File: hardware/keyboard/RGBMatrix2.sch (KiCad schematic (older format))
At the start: 29 parts

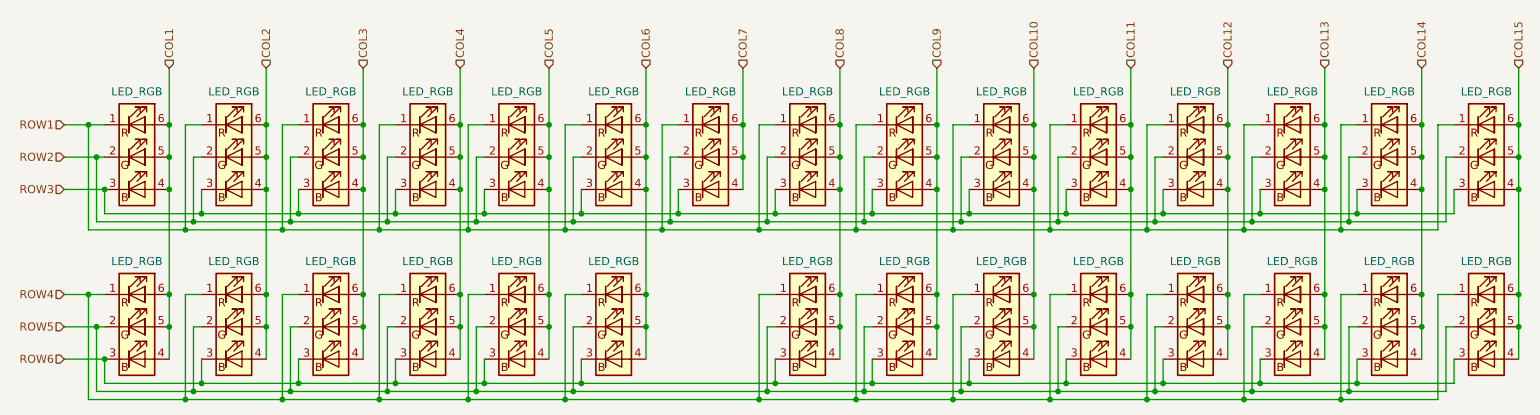
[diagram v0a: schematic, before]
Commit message: switch to proper type of RGB(Common anode)
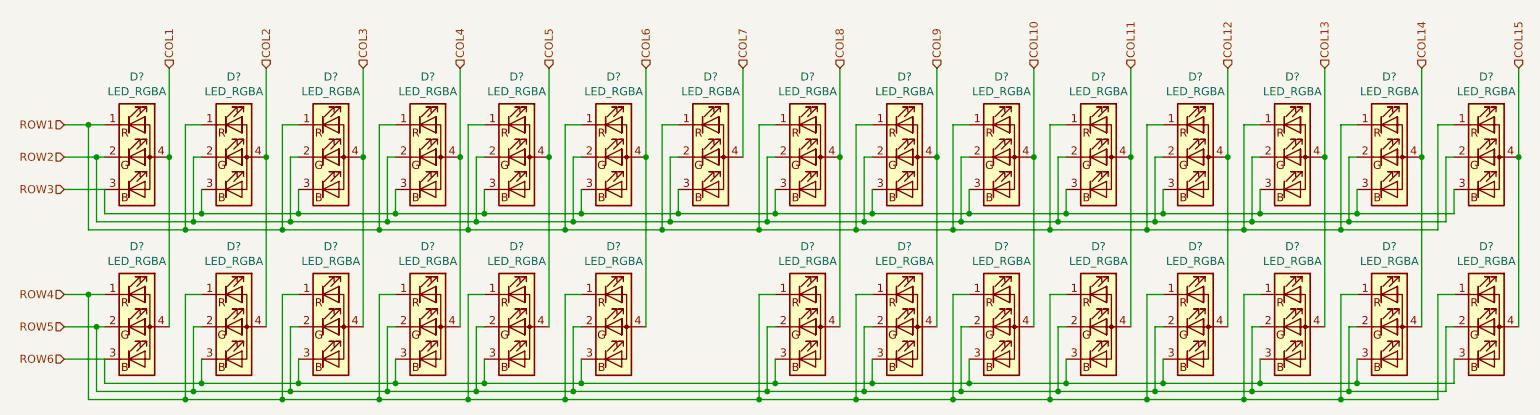
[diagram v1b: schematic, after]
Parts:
- removed D114, D115, D116, D117, D118, D119, D120, D121, D122, D123, D124, D125, D126, D128, D129, D130, D131, D132, D133, D134, D135, D136, D137, D138, D139, D140, D141, D142, D143: LED_RGB, symbol Device:LED_RGB
- added D? (x29): LED_RGBA, symbol Device:LED_RGBA
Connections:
- net COL1: now also D?.4 (A), D?.4 (A)
- net COL10: now also D?.4 (A), D?.4 (A)
- net COL11: now also D?.4 (A), D?.4 (A)
- net COL12: now also D?.4 (A), D?.4 (A)
- net COL13: now also D?.4 (A), D?.4 (A)
- net COL14: now also D?.4 (A), D?.4 (A)
- net COL15: now also D?.4 (A), D?.4 (A)
- net COL2: now also D?.4 (A), D?.4 (A)
- net COL3: now also D?.4 (A), D?.4 (A)
- net COL4: now also D?.4 (A), D?.4 (A)
- net COL5: now also D?.4 (A), D?.4 (A)
- net COL6: now also D?.4 (A), D?.4 (A)
- net COL7: now also D?.4 (A)
- net COL8: now also D?.4 (A), D?.4 (A)
- net COL9: now also D?.4 (A), D?.4 (A)
- net ROW1: now also D?.1 (RK), D?.1 (RK), D?.1 (RK), D?.1 (RK), D?.1 (RK), D?.1 (RK), D?.1 (RK), D?.1 (RK), D?.1 (RK), D?.1 (RK), D?.1 (RK), D?.1 (RK), D?.1 (RK), D?.1 (RK), D?.1 (RK)
- net ROW2: now also D?.2 (GK), D?.2 (GK), D?.2 (GK), D?.2 (GK), D?.2 (GK), D?.2 (GK), D?.2 (GK), D?.2 (GK), D?.2 (GK), D?.2 (GK), D?.2 (GK), D?.2 (GK), D?.2 (GK), D?.2 (GK), D?.2 (GK)
- net ROW3: now also D?.3 (BK), D?.3 (BK), D?.3 (BK), D?.3 (BK), D?.3 (BK), D?.3 (BK), D?.3 (BK), D?.3 (BK), D?.3 (BK), D?.3 (BK), D?.3 (BK), D?.3 (BK), D?.3 (BK), D?.3 (BK), D?.3 (BK)
- net ROW4: now also D?.1 (RK), D?.1 (RK), D?.1 (RK), D?.1 (RK), D?.1 (RK), D?.1 (RK), D?.1 (RK), D?.1 (RK), D?.1 (RK), D?.1 (RK), D?.1 (RK), D?.1 (RK), D?.1 (RK), D?.1 (RK)
- net ROW5: now also D?.2 (GK), D?.2 (GK), D?.2 (GK), D?.2 (GK), D?.2 (GK), D?.2 (GK), D?.2 (GK), D?.2 (GK), D?.2 (GK), D?.2 (GK), D?.2 (GK), D?.2 (GK), D?.2 (GK), D?.2 (GK)
- net ROW6: now also D?.3 (BK), D?.3 (BK), D?.3 (BK), D?.3 (BK), D?.3 (BK), D?.3 (BK), D?.3 (BK), D?.3 (BK), D?.3 (BK), D?.3 (BK), D?.3 (BK), D?.3 (BK), D?.3 (BK), D?.3 (BK)

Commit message: fix unconnected rgb
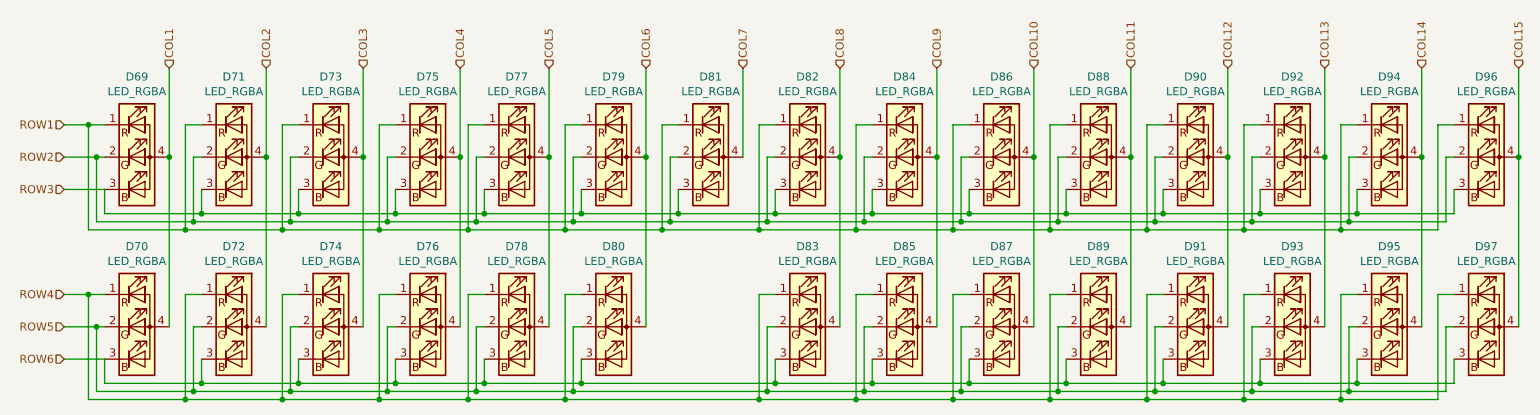
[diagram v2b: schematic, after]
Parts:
- gave numbers to parts that had none: 29
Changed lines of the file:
@@
 U 1 1 5ECE6F4E
 P 1750 2400
-F 0 "D?" H 1750 2897 50  0000 C CNN
+AR Path="/5EC33E3D/5EC48B37/5ECE6F4E" Ref="D?"  Part="1"
+AR Path="/5EC33E3D/5E12F961/5ECE6F4E" Ref="D69"  Part="1"
+F 0 "D69" H 1750 2897 50  0000 C CNN
 F 1 "LED_RGBA" H 1750 2806 50  0000 C CNN
 F 2 "" H 1750 2350 50  0001 C CNN
@@
 U 1 1 5ECF7D8D
 P 2350 2400
-F 0 "D?" H 2350 2897 50  0000 C CNN
+AR Path="/5EC33E3D/5EC48B37/5ECF7D8D" Ref="D?"  Part="1"
+AR Path="/5EC33E3D/5E12F961/5ECF7D8D" Ref="D71"  Part="1"
+F 0 "D71" H 2350 2897 50  0000 C CNN
 F 1 "LED_RGBA" H 2350 2806 50  0000 C CNN
 F 2 "" H 2350 2350 50  0001 C CNN
@@
 U 1 1 5ED08C1C
 P 2950 2400
-F 0 "D?" H 2950 2897 50  0000 C CNN
+AR Path="/5EC33E3D/5EC48B37/5ED08C1C" Ref="D?"  Part="1"
+AR Path="/5EC33E3D/5E12F961/5ED08C1C" Ref="D73"  Part="1"
+F 0 "D73" H 2950 2897 50  0000 C CNN
 F 1 "LED_RGBA" H 2950 2806 50  0000 C CNN
 F 2 "" H 2950 2350 50  0001 C CNN
@@
 U 1 1 5ED19532
 P 3550 2400
-F 0 "D?" H 3550 2897 50  0000 C CNN
+AR Path="/5EC33E3D/5EC48B37/5ED19532" Ref="D?"  Part="1"
+AR Path="/5EC33E3D/5E12F961/5ED19532" Ref="D75"  Part="1"
+F 0 "D75" H 3550 2897 50  0000 C CNN
 F 1 "LED_RGBA" H 3550 2806 50  0000 C CNN
 F 2 "" H 3550 2350 50  0001 C CNN
@@
 U 1 1 5ED2A1D2
 P 4100 2400
-F 0 "D?" H 4100 2897 50  0000 C CNN
+AR Path="/5EC33E3D/5EC48B37/5ED2A1D2" Ref="D?"  Part="1"
+AR Path="/5EC33E3D/5E12F961/5ED2A1D2" Ref="D77"  Part="1"
+F 0 "D77" H 4100 2897 50  0000 C CNN
 F 1 "LED_RGBA" H 4100 2806 50  0000 C CNN
 F 2 "" H 4100 2350 50  0001 C CNN
@@
 U 1 1 5ED3AE35
 P 4700 2400
-F 0 "D?" H 4700 2897 50  0000 C CNN
+AR Path="/5EC33E3D/5EC48B37/5ED3AE35" Ref="D?"  Part="1"
+AR Path="/5EC33E3D/5E12F961/5ED3AE35" Ref="D79"  Part="1"
+F 0 "D79" H 4700 2897 50  0000 C CNN
 F 1 "LED_RGBA" H 4700 2806 50  0000 C CNN
 F 2 "" H 4700 2350 50  0001 C CNN
@@
 U 1 1 5ED4B8F9
 P 5300 2400
-F 0 "D?" H 5300 2897 50  0000 C CNN
+AR Path="/5EC33E3D/5EC48B37/5ED4B8F9" Ref="D?"  Part="1"
+AR Path="/5EC33E3D/5E12F961/5ED4B8F9" Ref="D81"  Part="1"
+F 0 "D81" H 5300 2897 50  0000 C CNN
 F 1 "LED_RGBA" H 5300 2806 50  0000 C CNN
 F 2 "" H 5300 2350 50  0001 C CNN
@@
 U 1 1 5ED5C37B
 P 5900 2400
-F 0 "D?" H 5900 2897 50  0000 C CNN
+AR Path="/5EC33E3D/5EC48B37/5ED5C37B" Ref="D?"  Part="1"
+AR Path="/5EC33E3D/5E12F961/5ED5C37B" Ref="D82"  Part="1"
+F 0 "D82" H 5900 2897 50  0000 C CNN
 F 1 "LED_RGBA" H 5900 2806 50  0000 C CNN
 F 2 "" H 5900 2350 50  0001 C CNN
@@
 U 1 1 5ED6CA4B
 P 6500 2400
-F 0 "D?" H 6500 2897 50  0000 C CNN
+AR Path="/5EC33E3D/5EC48B37/5ED6CA4B" Ref="D?"  Part="1"
+AR Path="/5EC33E3D/5E12F961/5ED6CA4B" Ref="D84"  Part="1"
+F 0 "D84" H 6500 2897 50  0000 C CNN
 F 1 "LED_RGBA" H 6500 2806 50  0000 C CNN
 F 2 "" H 6500 2350 50  0001 C CNN
@@
 U 1 1 5ED7D671
 P 7100 2400
-F 0 "D?" H 7100 2897 50  0000 C CNN
+AR Path="/5EC33E3D/5EC48B37/5ED7D671" Ref="D?"  Part="1"
+AR Path="/5EC33E3D/5E12F961/5ED7D671" Ref="D86"  Part="1"
+F 0 "D86" H 7100 2897 50  0000 C CNN
 F 1 "LED_RGBA" H 7100 2806 50  0000 C CNN
 F 2 "" H 7100 2350 50  0001 C CNN
@@
 U 1 1 5ED8E3BC
 P 7700 2400
-F 0 "D?" H 7700 2897 50  0000 C CNN
+AR Path="/5EC33E3D/5EC48B37/5ED8E3BC" Ref="D?"  Part="1"
+AR Path="/5EC33E3D/5E12F961/5ED8E3BC" Ref="D88"  Part="1"
+F 0 "D88" H 7700 2897 50  0000 C CNN
 F 1 "LED_RGBA" H 7700 2806 50  0000 C CNN
 F 2 "" H 7700 2350 50  0001 C CNN
@@
 U 1 1 5ED9EECC
 P 8300 2400
-F 0 "D?" H 8300 2897 50  0000 C CNN
+AR Path="/5EC33E3D/5EC48B37/5ED9EECC" Ref="D?"  Part="1"
+AR Path="/5EC33E3D/5E12F961/5ED9EECC" Ref="D90"  Part="1"
+F 0 "D90" H 8300 2897 50  0000 C CNN
 F 1 "LED_RGBA" H 8300 2806 50  0000 C CNN
 F 2 "" H 8300 2350 50  0001 C CNN
@@
 U 1 1 5EDAF8D0
 P 8900 2400
-F 0 "D?" H 8900 2897 50  0000 C CNN
+AR Path="/5EC33E3D/5EC48B37/5EDAF8D0" Ref="D?"  Part="1"
+AR Path="/5EC33E3D/5E12F961/5EDAF8D0" Ref="D92"  Part="1"
+F 0 "D92" H 8900 2897 50  0000 C CNN
 F 1 "LED_RGBA" H 8900 2806 50  0000 C CNN
 F 2 "" H 8900 2350 50  0001 C CNN
@@
 U 1 1 5EDC0468
 P 9500 2400
-F 0 "D?" H 9500 2897 50  0000 C CNN
+AR Path="/5EC33E3D/5EC48B37/5EDC0468" Ref="D?"  Part="1"
+AR Path="/5EC33E3D/5E12F961/5EDC0468" Ref="D94"  Part="1"
+F 0 "D94" H 9500 2897 50  0000 C CNN
 F 1 "LED_RGBA" H 9500 2806 50  0000 C CNN
 F 2 "" H 9500 2350 50  0001 C CNN
@@
 U 1 1 5EDD0EEE
 P 10100 2400
-F 0 "D?" H 10100 2897 50  0000 C CNN
+AR Path="/5EC33E3D/5EC48B37/5EDD0EEE" Ref="D?"  Part="1"
+AR Path="/5EC33E3D/5E12F961/5EDD0EEE" Ref="D96"  Part="1"
+F 0 "D96" H 10100 2897 50  0000 C CNN
 F 1 "LED_RGBA" H 10100 2806 50  0000 C CNN
 F 2 "" H 10100 2350 50  0001 C CNN
@@
 U 1 1 5EDE1C35
 P 10100 3450
-F 0 "D?" H 10100 3947 50  0000 C CNN
+AR Path="/5EC33E3D/5EC48B37/5EDE1C35" Ref="D?"  Part="1"
+AR Path="/5EC33E3D/5E12F961/5EDE1C35" Ref="D97"  Part="1"
+F 0 "D97" H 10100 3947 50  0000 C CNN
 F 1 "LED_RGBA" H 10100 3856 50  0000 C CNN
 F 2 "" H 10100 3400 50  0001 C CNN
@@
 U 1 1 5EDF2634
 P 9500 3450
-F 0 "D?" H 9500 3947 50  0000 C CNN
+AR Path="/5EC33E3D/5EC48B37/5EDF2634" Ref="D?"  Part="1"
+AR Path="/5EC33E3D/5E12F961/5EDF2634" Ref="D95"  Part="1"
+F 0 "D95" H 9500 3947 50  0000 C CNN
 F 1 "LED_RGBA" H 9500 3856 50  0000 C CNN
 F 2 "" H 9500 3400 50  0001 C CNN
@@
 U 1 1 5EE030A2
 P 8900 3450
-F 0 "D?" H 8900 3947 50  0000 C CNN
+AR Path="/5EC33E3D/5EC48B37/5EE030A2" Ref="D?"  Part="1"
+AR Path="/5EC33E3D/5E12F961/5EE030A2" Ref="D93"  Part="1"
+F 0 "D93" H 8900 3947 50  0000 C CNN
 F 1 "LED_RGBA" H 8900 3856 50  0000 C CNN
 F 2 "" H 8900 3400 50  0001 C CNN
@@
 U 1 1 5EE13AA6
 P 8300 3450
-F 0 "D?" H 8300 3947 50  0000 C CNN
+AR Path="/5EC33E3D/5EC48B37/5EE13AA6" Ref="D?"  Part="1"
+AR Path="/5EC33E3D/5E12F961/5EE13AA6" Ref="D91"  Part="1"
+F 0 "D91" H 8300 3947 50  0000 C CNN
 F 1 "LED_RGBA" H 8300 3856 50  0000 C CNN
 F 2 "" H 8300 3400 50  0001 C CNN
@@
 U 1 1 5EE24547
 P 7700 3450
-F 0 "D?" H 7700 3947 50  0000 C CNN
+AR Path="/5EC33E3D/5EC48B37/5EE24547" Ref="D?"  Part="1"
+AR Path="/5EC33E3D/5E12F961/5EE24547" Ref="D89"  Part="1"
+F 0 "D89" H 7700 3947 50  0000 C CNN
 F 1 "LED_RGBA" H 7700 3856 50  0000 C CNN
 F 2 "" H 7700 3400 50  0001 C CNN
@@
 U 1 1 5EE34C17
 P 7100 3450
-F 0 "D?" H 7100 3947 50  0000 C CNN
+AR Path="/5EC33E3D/5EC48B37/5EE34C17" Ref="D?"  Part="1"
+AR Path="/5EC33E3D/5E12F961/5EE34C17" Ref="D87"  Part="1"
+F 0 "D87" H 7100 3947 50  0000 C CNN
 F 1 "LED_RGBA" H 7100 3856 50  0000 C CNN
 F 2 "" H 7100 3400 50  0001 C CNN
@@
 U 1 1 5EE45875
 P 6500 3450
-F 0 "D?" H 6500 3947 50  0000 C CNN
+AR Path="/5EC33E3D/5EC48B37/5EE45875" Ref="D?"  Part="1"
+AR Path="/5EC33E3D/5E12F961/5EE45875" Ref="D85"  Part="1"
+F 0 "D85" H 6500 3947 50  0000 C CNN
 F 1 "LED_RGBA" H 6500 3856 50  0000 C CNN
 F 2 "" H 6500 3400 50  0001 C CNN
@@
 U 1 1 5EE56B5B
 P 5900 3450
-F 0 "D?" H 5900 3947 50  0000 C CNN
+AR Path="/5EC33E3D/5EC48B37/5EE56B5B" Ref="D?"  Part="1"
+AR Path="/5EC33E3D/5E12F961/5EE56B5B" Ref="D83"  Part="1"
+F 0 "D83" H 5900 3947 50  0000 C CNN
 F 1 "LED_RGBA" H 5900 3856 50  0000 C CNN
 F 2 "" H 5900 3400 50  0001 C CNN
@@
 U 1 1 5EE68DA5
 P 4700 3450
-F 0 "D?" H 4700 3947 50  0000 C CNN
+AR Path="/5EC33E3D/5EC48B37/5EE68DA5" Ref="D?"  Part="1"
+AR Path="/5EC33E3D/5E12F961/5EE68DA5" Ref="D80"  Part="1"
+F 0 "D80" H 4700 3947 50  0000 C CNN
 F 1 "LED_RGBA" H 4700 3856 50  0000 C CNN
 F 2 "" H 4700 3400 50  0001 C CNN
@@
 U 1 1 5EE797FA
 P 4100 3450
-F 0 "D?" H 4100 3947 50  0000 C CNN
+AR Path="/5EC33E3D/5EC48B37/5EE797FA" Ref="D?"  Part="1"
+AR Path="/5EC33E3D/5E12F961/5EE797FA" Ref="D78"  Part="1"
+F 0 "D78" H 4100 3947 50  0000 C CNN
 F 1 "LED_RGBA" H 4100 3856 50  0000 C CNN
 F 2 "" H 4100 3400 50  0001 C CNN
@@
 U 1 1 5EE8A2F6
 P 3550 3450
-F 0 "D?" H 3550 3947 50  0000 C CNN
+AR Path="/5EC33E3D/5EC48B37/5EE8A2F6" Ref="D?"  Part="1"
+AR Path="/5EC33E3D/5E12F961/5EE8A2F6" Ref="D76"  Part="1"
+F 0 "D76" H 3550 3947 50  0000 C CNN
 F 1 "LED_RGBA" H 3550 3856 50  0000 C CNN
 F 2 "" H 3550 3400 50  0001 C CNN
@@
 U 1 1 5EEAC0EB
 P 2950 3450
-F 0 "D?" H 2950 3947 50  0000 C CNN
+AR Path="/5EC33E3D/5EC48B37/5EEAC0EB" Ref="D?"  Part="1"
+AR Path="/5EC33E3D/5E12F961/5EEAC0EB" Ref="D74"  Part="1"
+F 0 "D74" H 2950 3947 50  0000 C CNN
 F 1 "LED_RGBA" H 2950 3856 50  0000 C CNN
 F 2 "" H 2950 3400 50  0001 C CNN
@@
 U 1 1 5EEBC7BB
 P 2350 3450
-F 0 "D?" H 2350 3947 50  0000 C CNN
+AR Path="/5EC33E3D/5EC48B37/5EEBC7BB" Ref="D?"  Part="1"
+AR Path="/5EC33E3D/5E12F961/5EEBC7BB" Ref="D72"  Part="1"
+F 0 "D72" H 2350 3947 50  0000 C CNN
 F 1 "LED_RGBA" H 2350 3856 50  0000 C CNN
 F 2 "" H 2350 3400 50  0001 C CNN
@@
 U 1 1 5EECD5B2
 P 1750 3450
-F 0 "D?" H 1750 3947 50  0000 C CNN
+AR Path="/5EC33E3D/5EC48B37/5EECD5B2" Ref="D?"  Part="1"
+AR Path="/5EC33E3D/5E12F961/5EECD5B2" Ref="D70"  Part="1"
+F 0 "D70" H 1750 3947 50  0000 C CNN
 F 1 "LED_RGBA" H 1750 3856 50  0000 C CNN
 F 2 "" H 1750 3400 50  0001 C CNN

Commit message: now it should be using the correct rgb symbol (RABG)
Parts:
- D69, D70, D71, D72, D73, D74, D75, D76, D77, D78, D79, D80, D81, D82, D83, D84, D85, D86, D87, D88, D89, D90, D91, D92, D93, D94, D95, D96, D97: value LED_RGBA -> LED_RABG; symbol Device:LED_RGBA -> Device:LED_RABG
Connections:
- net COL1: now also D69.2 (A), D70.2 (A); no longer D69.4 (A), D70.4 (A)
- net COL10: now also D86.2 (A), D87.2 (A); no longer D86.4 (A), D87.4 (A)
- net COL11: now also D88.2 (A), D89.2 (A); no longer D88.4 (A), D89.4 (A)
- net COL12: now also D90.2 (A), D91.2 (A); no longer D90.4 (A), D91.4 (A)
- net COL13: now also D92.2 (A), D93.2 (A); no longer D92.4 (A), D93.4 (A)
- net COL14: now also D94.2 (A), D95.2 (A); no longer D94.4 (A), D95.4 (A)
- net COL15: now also D96.2 (A), D97.2 (A); no longer D96.4 (A), D97.4 (A)
- net COL2: now also D71.2 (A), D72.2 (A); no longer D71.4 (A), D72.4 (A)
- net COL3: now also D73.2 (A), D74.2 (A); no longer D73.4 (A), D74.4 (A)
- net COL4: now also D75.2 (A), D76.2 (A); no longer D75.4 (A), D76.4 (A)
- net COL5: now also D77.2 (A), D78.2 (A); no longer D77.4 (A), D78.4 (A)
- net COL6: now also D79.2 (A), D80.2 (A); no longer D79.4 (A), D80.4 (A)
- net COL7: now also D81.2 (A); no longer D81.4 (A)
- net COL8: now also D82.2 (A), D83.2 (A); no longer D82.4 (A), D83.4 (A)
- net COL9: now also D84.2 (A), D85.2 (A); no longer D84.4 (A), D85.4 (A)
- net ROW2: now also D69.4 (GK), D71.4 (GK), D73.4 (GK), D75.4 (GK), D77.4 (GK), D79.4 (GK), D81.4 (GK), D82.4 (GK), D84.4 (GK), D86.4 (GK), D88.4 (GK), D90.4 (GK), D92.4 (GK), D94.4 (GK), D96.4 (GK); no longer D69.2 (GK), D71.2 (GK), D73.2 (GK), D75.2 (GK), D77.2 (GK), D79.2 (GK), D81.2 (GK), D82.2 (GK), D84.2 (GK), D86.2 (GK), D88.2 (GK), D90.2 (GK), D92.2 (GK), D94.2 (GK), D96.2 (GK)
- net ROW5: now also D70.4 (GK), D72.4 (GK), D74.4 (GK), D76.4 (GK), D78.4 (GK), D80.4 (GK), D83.4 (GK), D85.4 (GK), D87.4 (GK), D89.4 (GK), D91.4 (GK), D93.4 (GK), D95.4 (GK), D97.4 (GK); no longer D70.2 (GK), D72.2 (GK), D74.2 (GK), D76.2 (GK), D78.2 (GK), D80.2 (GK), D83.2 (GK), D85.2 (GK), D87.2 (GK), D89.2 (GK), D91.2 (GK), D93.2 (GK), D95.2 (GK), D97.2 (GK)
